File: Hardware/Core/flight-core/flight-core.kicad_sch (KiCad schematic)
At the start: 20 parts, among them J1 Conn_02x02_Remote_ESTOP, J2 Conn_02x04_Counter_Clockwise, J3 Conn_02x05_Counter_Clockwise, J4 Conn_02x05_Counter_Clockwise, J5 Conn_02x05_Counter_Clockwise, J6 Conn_02x05_Counter_Clockwise

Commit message: Major reroute & semi-final update
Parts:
- removed J2: Conn_02x04_Counter_Clockwise, obad_footprints:MicroFit_VT_8, symbol Connector_Generic:Conn_02x04_Counter_Clockwise
- added H101, H102, H103, H104, H105, H106, H107, H108: MountingHole_Pad, MountingHole:MountingHole_3.2mm_M3_Pad_Via, symbol Mechanical:MountingHole_Pad
- added J101: Conn_02x05_Counter_Clockwise, Connector_Molex:Molex_Micro-Fit_3.0_43045-1012_2x05_P3.00mm_Vertical, symbol Connector_Generic:Conn_02x05_Counter_Clockwise
- J1: value Conn_02x02_Remote_ESTOP -> Conn_02x02_GPS
- TP1, TP2, TP3, TP4, TP5, TP6: footprint footprints:Test_Point_SMD -> TestPoint:TestPoint_Keystone_5019_Miniature
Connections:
- net +5V: now also J101.1 (Pin_1)
- net +BATT: now also J101.10 (Pin_10)
- net CAN+_SENSE: now also J101.8 (Pin_8)
- net CAN-_SENSE: now also J101.7 (Pin_7)
- net GND: now also H101.1, H102.1, H103.1, H104.1, H105.1, H106.1, H107.1, H108.1, J101.9 (Pin_9)
- net GPIO_SENSE1: now also J101.3 (Pin_3)
- net GPIO_SENSE2: now also J101.4 (Pin_4)
- net SENSE_POWER_CYCLE: now also J101.2 (Pin_2)
- net SHDN_SENSE_ALL_BATT: now also J6.8 (Pin_8); no longer J6.7 (Pin_7)
- net SHDN_SENSE_BMS_OK_E: now also J4.8 (Pin_8), J5.7 (Pin_7); no longer J4.7 (Pin_7), J5.8 (Pin_8)
- net SHDN_SENSE_BMS_OK_N: now also J3.8 (Pin_8), J4.7 (Pin_7); no longer J3.7 (Pin_7), J4.8 (Pin_8)
- net SHDN_SENSE_BMS_OK_S: now also J5.8 (Pin_8), J6.7 (Pin_7); no longer J5.7 (Pin_7), J6.8 (Pin_8)
- net SHDN_SENSE_NUC: now also J3.7 (Pin_7), J101.5 (Pin_5); no longer J3.8 (Pin_8)
- new net SHDN_SENSE_CTRL_LOBATT: J101.6 (Pin_6)
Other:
- sheet Shutdown Nodes ports: added none; removed SHDN_SENSE_NUC

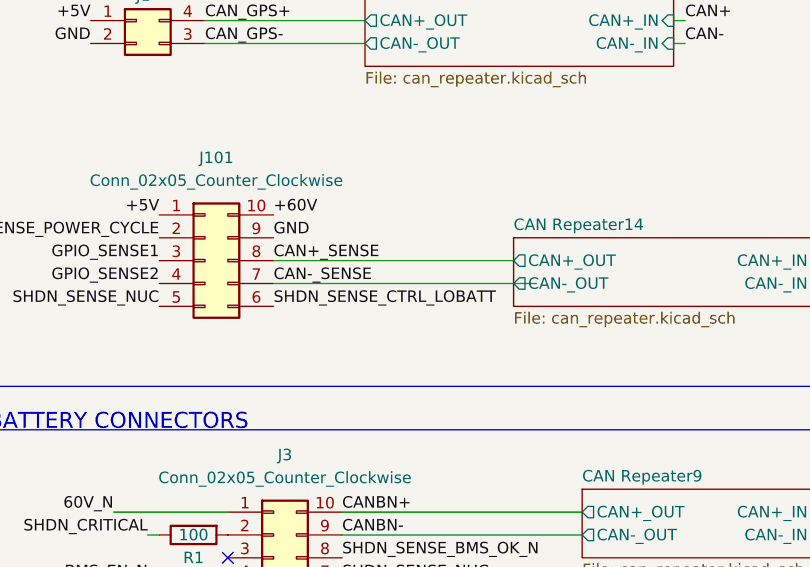
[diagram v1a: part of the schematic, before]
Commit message: moving silkscreen, renaming can repeater sheet name
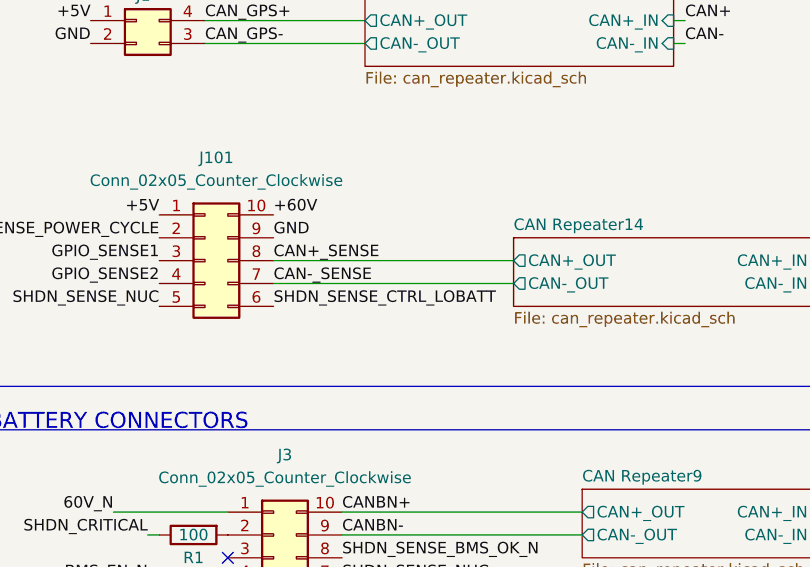
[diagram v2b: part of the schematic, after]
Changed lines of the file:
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@@
 	(wire
 		(pts
-			(xy 50.8 62.23) (xy 80.01 62.23)
+			(xy 170.18 87.63) (xy 213.36 87.63)
 		)
 		(stroke
@@
 	(wire
 		(pts
-			(xy 170.18 87.63) (xy 213.36 87.63)
+			(xy 177.8 41.91) (xy 185.42 41.91)
 		)
 		(stroke
@@
 	(wire
 		(pts
-			(xy 177.8 41.91) (xy 185.42 41.91)
+			(xy 43.18 35.56) (xy 60.96 35.56)
 		)
 		(stroke
@@
 	(wire
 		(pts
-			(xy 43.18 35.56) (xy 60.96 35.56)
+			(xy 217.17 144.78) (xy 219.71 144.78)
 		)
 		(stroke
@@
 	(wire
 		(pts
-			(xy 217.17 144.78) (xy 219.71 144.78)
+			(xy 36.83 95.25) (xy 45.72 95.25)
 		)
 		(stroke
@@
 	(wire
 		(pts
-			(xy 36.83 95.25) (xy 45.72 95.25)
+			(xy 58.42 156.21) (xy 85.09 156.21)
 		)
 		(stroke
@@
 	(wire
 		(pts
-			(xy 58.42 156.21) (xy 85.09 156.21)
+			(xy 50.8 62.23) (xy 77.47 62.23)
 		)
 		(stroke
@@
 					(size 1.27 1.27)
 				)
-				(justify right)
+				(justify left)
 			)
 		)
